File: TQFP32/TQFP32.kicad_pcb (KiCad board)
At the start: 2 copper layers, 53.3 x 20.6 mm, 2 parts, among them U1 ATmega8L-8AU

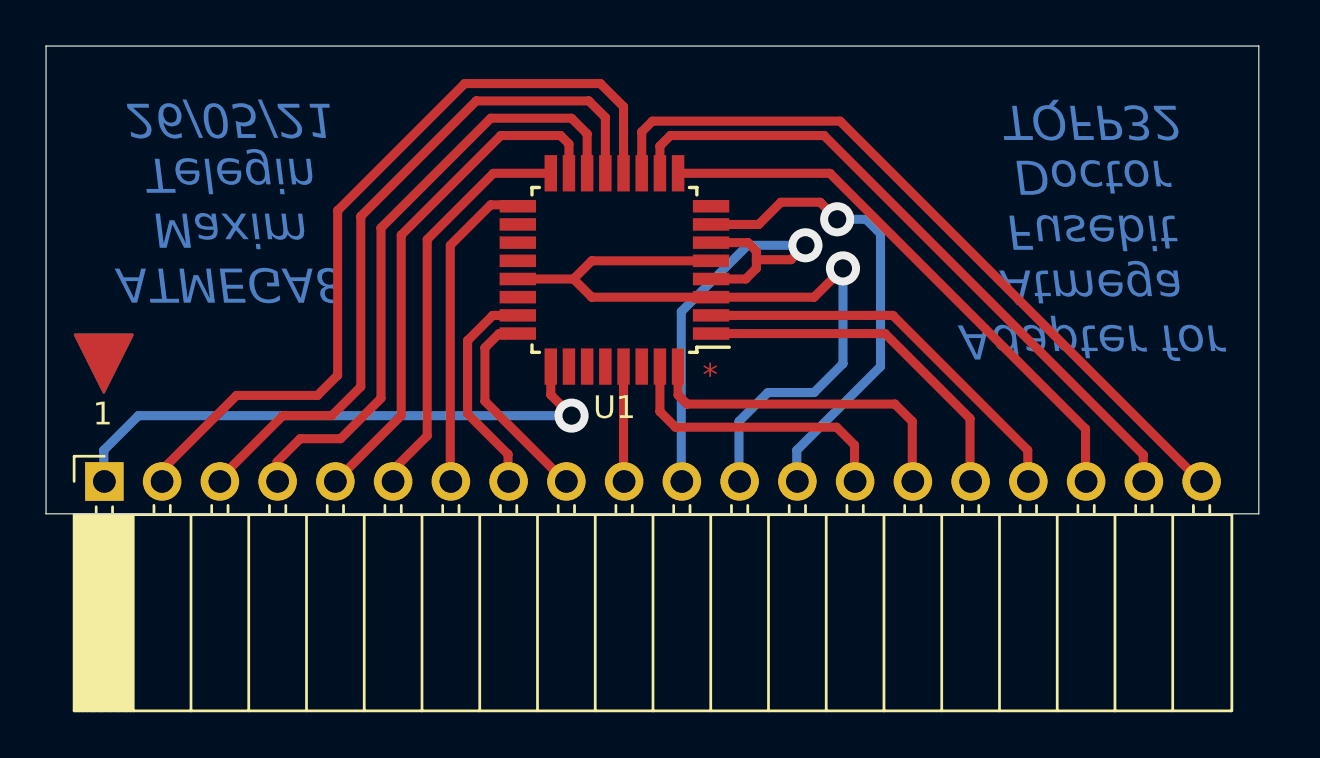
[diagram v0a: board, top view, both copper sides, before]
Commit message: Added ISP6 & LED for RESET & LED for POWER
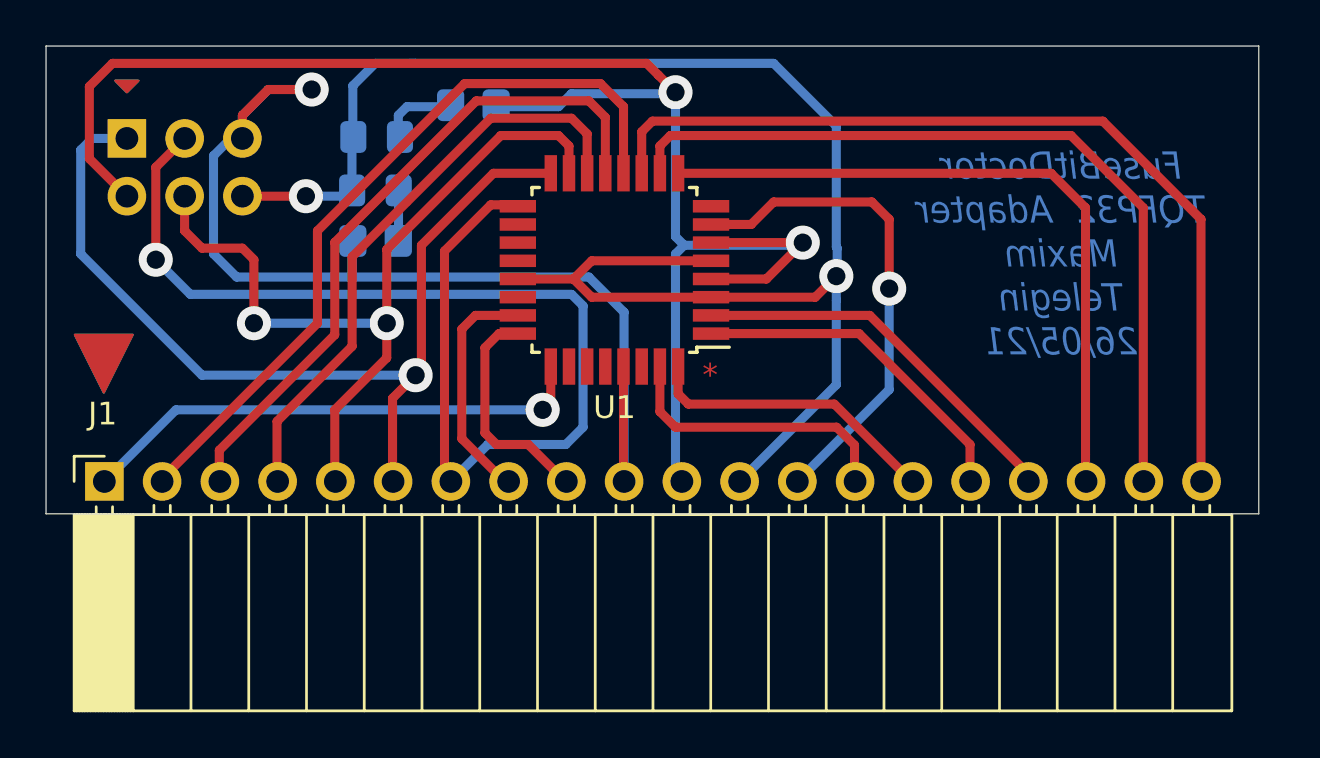
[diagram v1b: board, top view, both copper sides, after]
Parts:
- added D1: LED, LED_SMD:LED_0805_2012Metric_Pad1.15x1.40mm_HandSolder, B.Cu at (132.6, 100.3)
- added D2: LED, LED_SMD:LED_0805_2012Metric_Pad1.15x1.40mm_HandSolder, B.Cu at (132.7, 98.0)
- added J2: ISP, Connector_PinHeader_2.54mm:PinHeader_2x03_P2.54mm_Vertical, B.Cu at (121.7, 98.0)
- added R1: 1К, Resistor_SMD:R_0805_2012Metric_Pad1.20x1.40mm_HandSolder, B.Cu at (132.6, 102.6)
- added R2: 1К, Resistor_SMD:R_0805_2012Metric_Pad1.20x1.40mm_HandSolder, B.Cu at (136.9, 96.6)
- renumbered 1 to J1
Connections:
- net +12V_RESET renamed RESET
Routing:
- net +5V: track 21.7 -> 72.2 mm, vias 1 -> 2
- net RESET: track 5.08 -> 48.1 mm, vias 0 -> 1
- net DATA5: track 14.1 -> 52.5 mm, vias 0 -> 1
- net GND: track 34.0 -> 71.3 mm, vias 1 -> 2
- net DATA4: track 17.9 -> 41.7 mm, vias 0 -> 1
- net DATA3: track 22.7 -> 36.4 mm, vias 0 -> 2
- net PAG: track 33.2 -> 40.0 mm
- net XA1: track 29.7 -> 36.0 mm
- net XA0: track 24.9 -> 30.6 mm
- net Net-(D2-Pad1): track 0.00 -> 3.38 mm
- net BS2: track 25.1 -> 22.7 mm
- net Net-(D1-Pad1): track 0.00 -> 2.29 mm
- net DATA0: track 35.2 -> 33.2 mm
- net OE: track 14.7 -> 13.1 mm
- net DATA1: track 31.1 -> 29.9 mm
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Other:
- board text added: "FuseBitDoctor TQFP32 Adapter Maxim Telegin 26/05/21"
- board text removed: "ATMEGA8 Maxim Telegin 26/05/21"
- board text removed: "Adapter for Atmega Fusebit Doctor TQFP32"
